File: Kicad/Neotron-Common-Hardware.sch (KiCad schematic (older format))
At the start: 12 parts

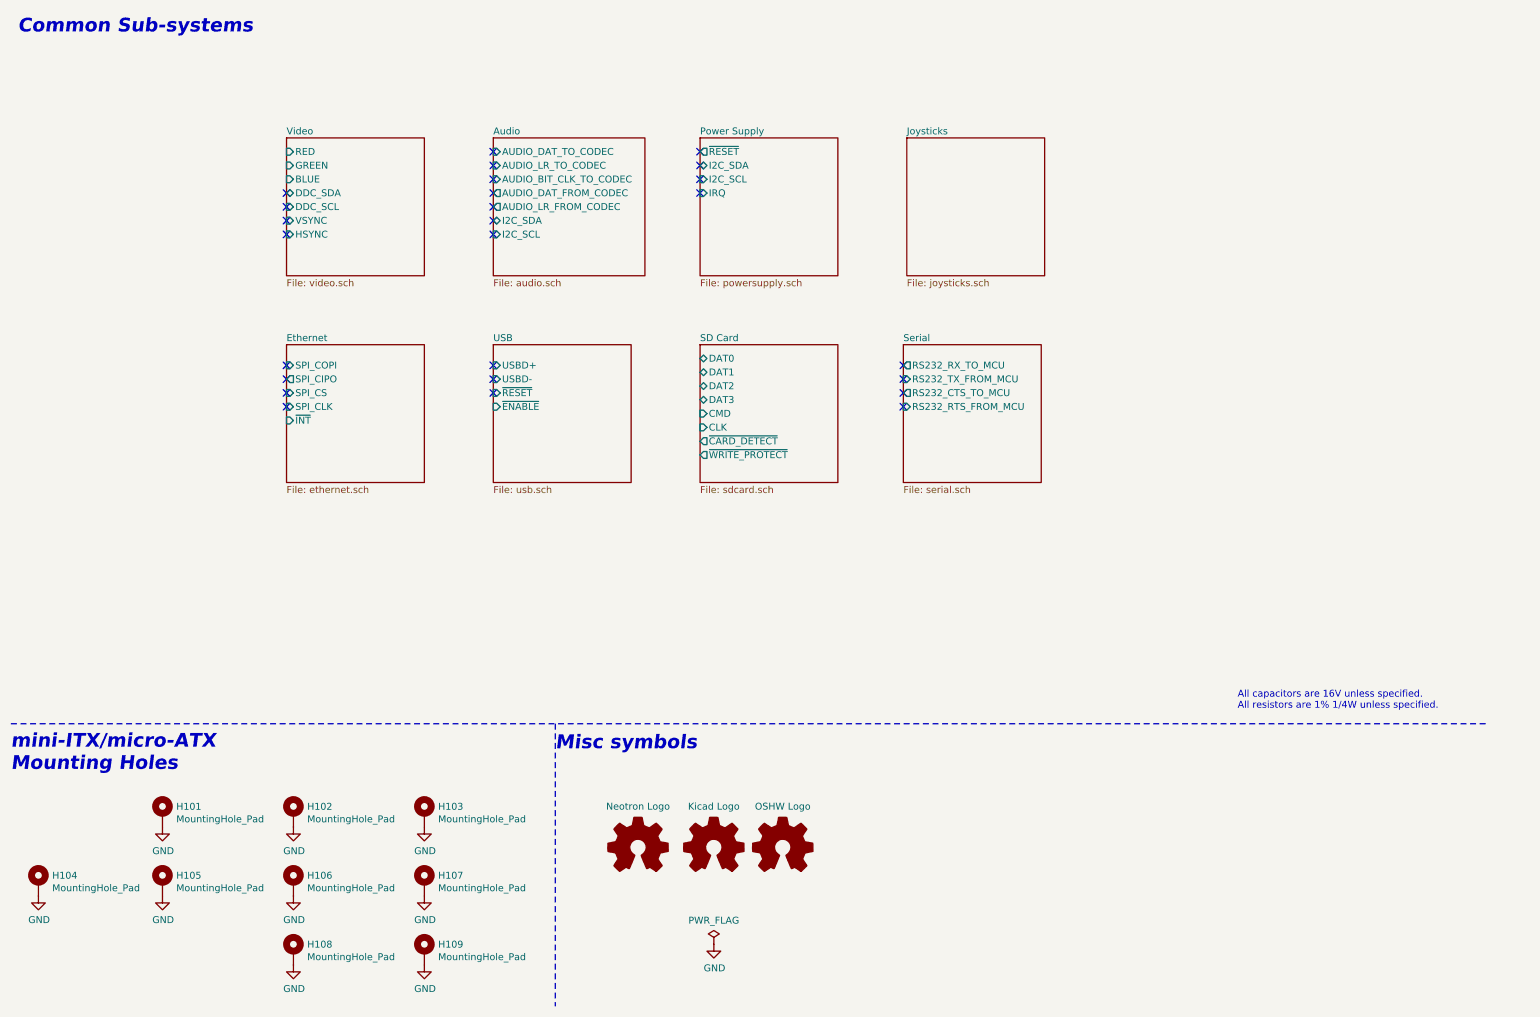
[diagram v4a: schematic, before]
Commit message: Make CPU card bigger.
Just big enough to take a TQFP-176 now.
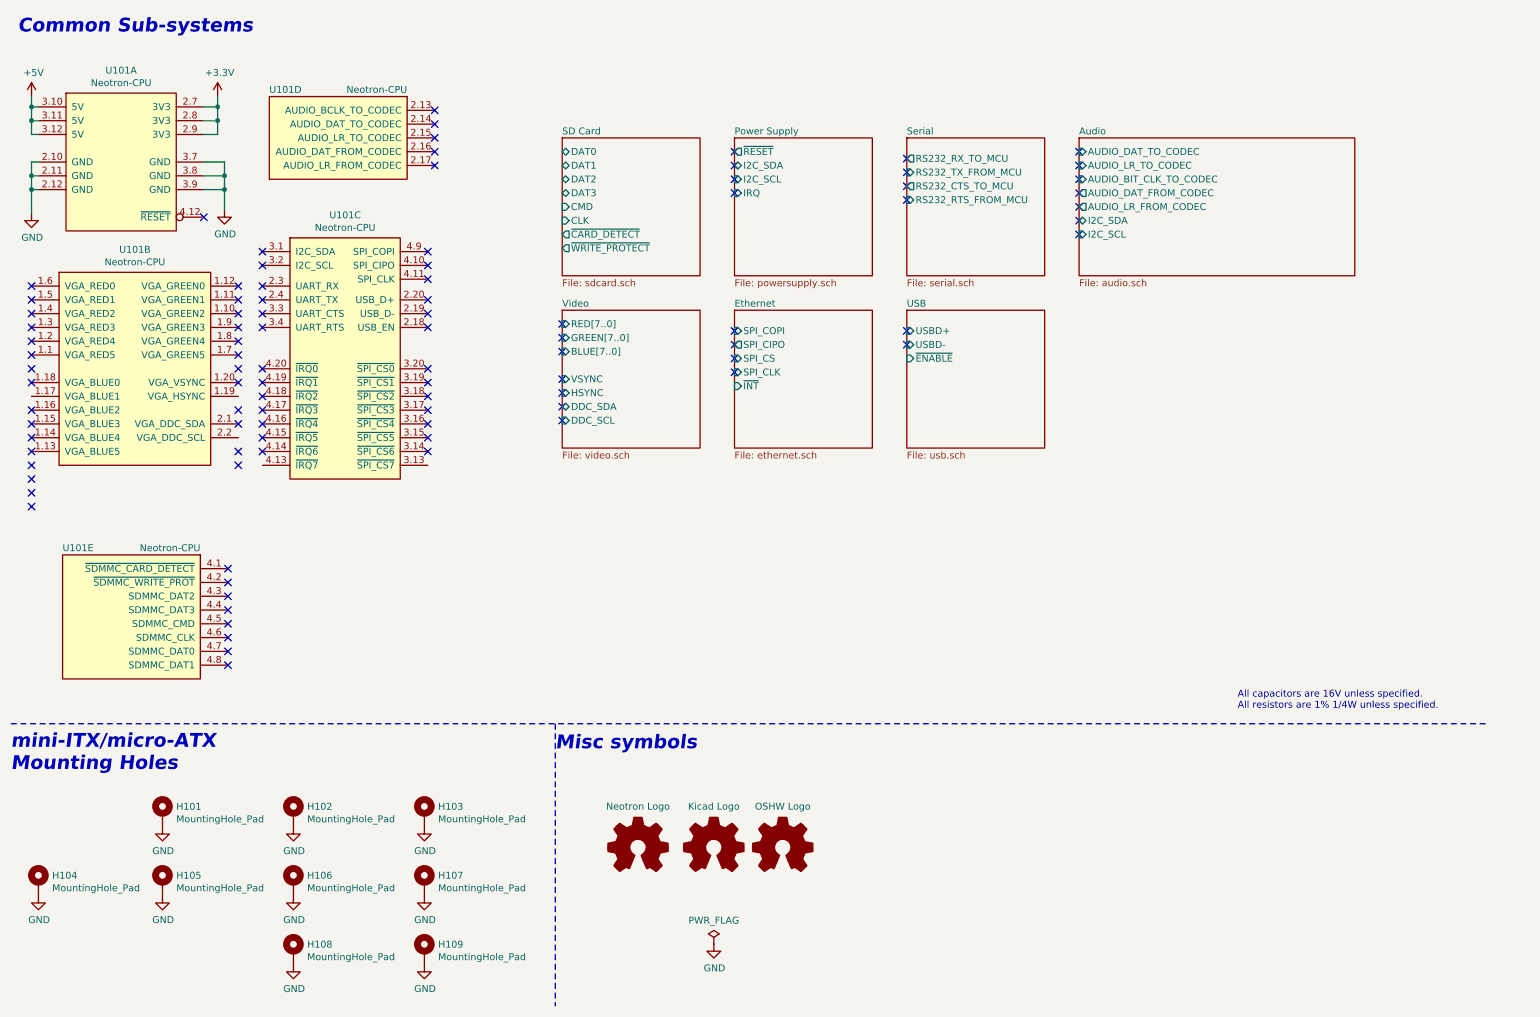
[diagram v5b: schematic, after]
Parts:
- added U101: Neotron-CPU, Neotron-Common-Hardware:Neotron_CPU_Socket, symbol Neotron-Common-Hardware:Neotron-CPU
- LOGO101, LOGO102, LOGO103: DNP 0 -> 1
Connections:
- net GND: now also U101.2.10 (GND), U101.2.11 (GND), U101.2.12 (GND), U101.3.7 (GND), U101.3.8 (GND), U101.3.9 (GND)
- new net +3V3: U101.2.7 (3V3), U101.2.8 (3V3), U101.2.9 (3V3)
- new net +5V: U101.3.10 (5V), U101.3.11 (5V), U101.3.12 (5V)
- no-connect marks 26 -> 96

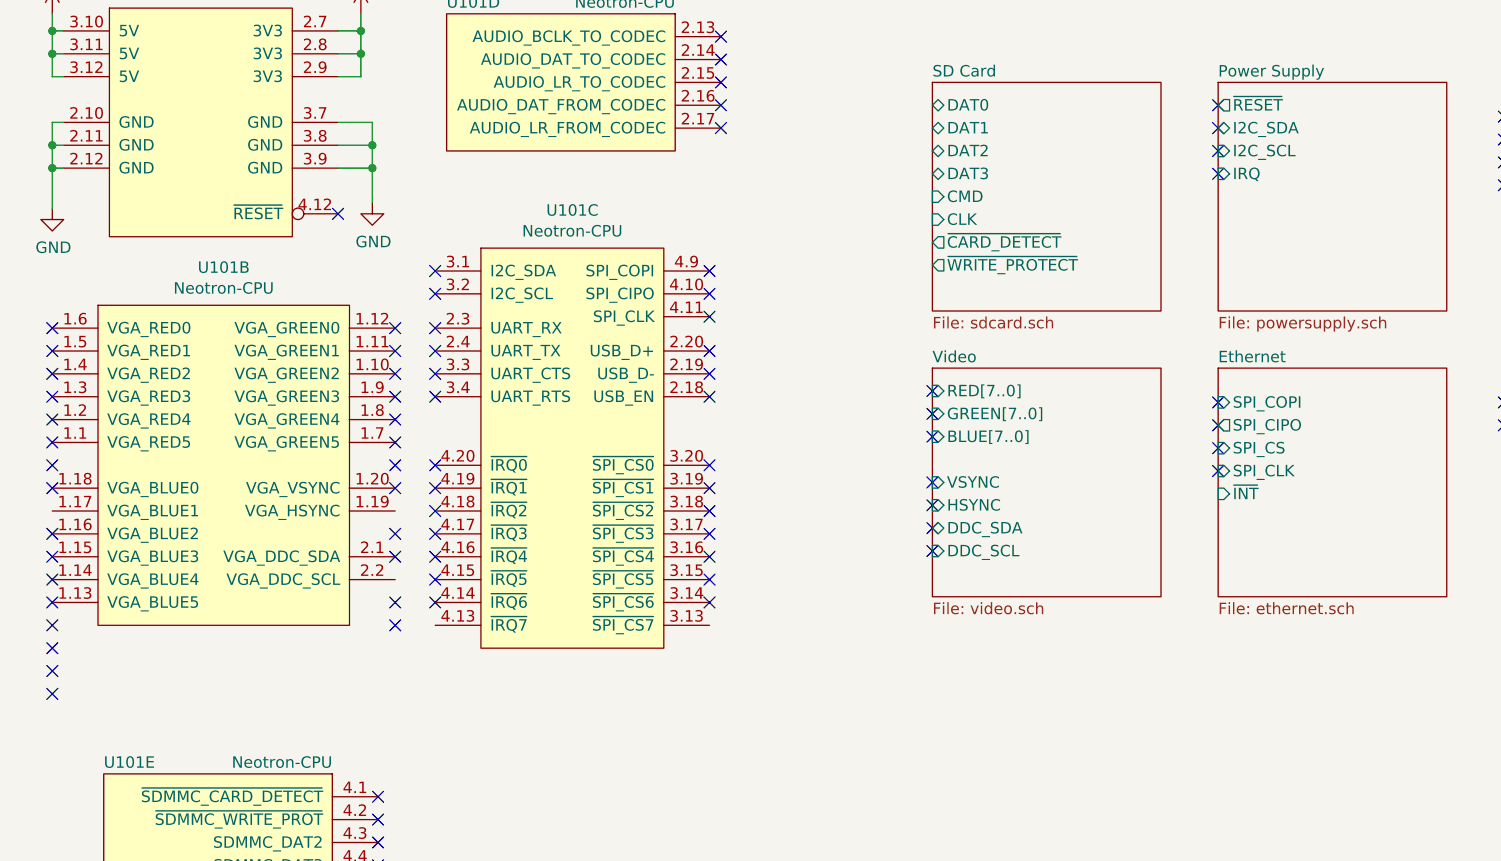
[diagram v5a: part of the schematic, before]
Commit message: Revised CPU connector to be two 2x20.
This gives more room for larger TQFP-176+ CPUs to be fitted that
didn't fit on the PGA-80 design.
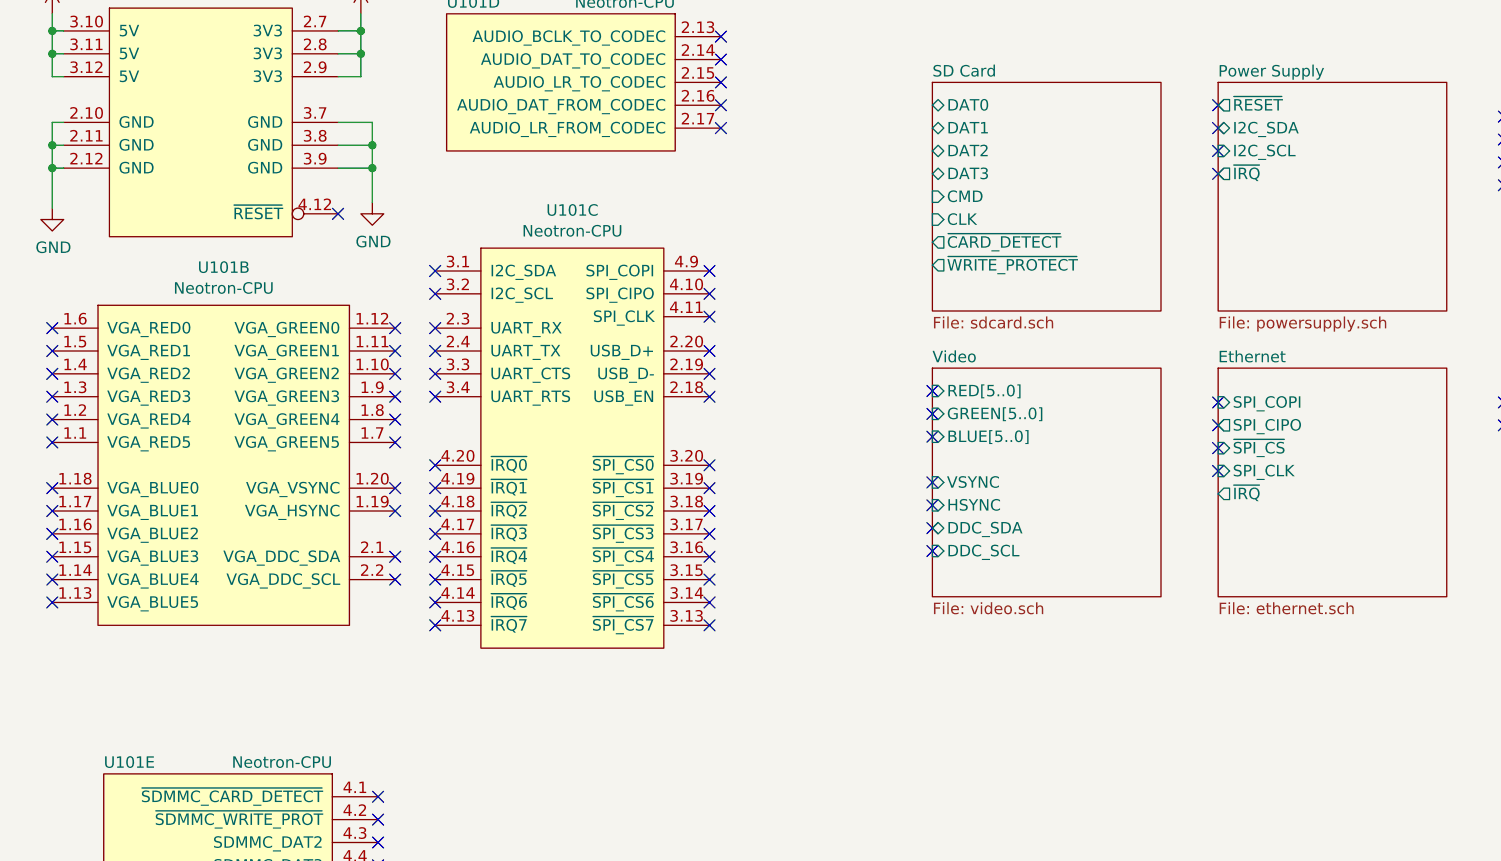
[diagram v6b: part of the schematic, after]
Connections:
- no-connect marks 96 -> 92
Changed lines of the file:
@@
 F4 "VSYNC" I L 4500 3250 50
 F5 "HSYNC" I L 4500 3350 50
-F6 "RED[7..0]" I L 4500 2850 50
-F7 "GREEN[7..0]" I L 4500 2950 50
-F8 "BLUE[7..0]" I L 4500 3050 50
+F6 "RED[5..0]" I L 4500 2850 50
+F7 "GREEN[5..0]" I L 4500 2950 50
+F8 "BLUE[5..0]" I L 4500 3050 50
 $EndSheet
 $Sheet
@@
 F3 "I2C_SDA" B L 5750 1700 50
 F4 "I2C_SCL" I L 5750 1800 50
-F5 "IRQ" I L 5750 1900 50
+F5 "~IRQ" O L 5750 1900 50
 $EndSheet
 $Sheet
@@
 F2 "SPI_COPI" I L 5750 2900 50
 F3 "SPI_CIPO" O L 5750 3000 50
-F4 "SPI_CS" I L 5750 3100 50
+F4 "~SPI_CS" I L 5750 3100 50
 F5 "SPI_CLK" I L 5750 3200 50
-F6 "~INT" I L 5750 3300 50
+F6 "~IRQ" O L 5750 3300 50
 $EndSheet
 $Comp
@@
 NoConn ~ 2150 2975
 NoConn ~ 2150 3075
-NoConn ~ 2150 3175
+NoConn ~ 2150 3375
 NoConn ~ 2150 3275
-NoConn ~ 2150 3475
 NoConn ~ 2150 3575
-NoConn ~ 2150 3775
-NoConn ~ 2150 3875
 NoConn ~ 650  2575
 NoConn ~ 650  2675
@@
 NoConn ~ 650  2975
 NoConn ~ 650  3075
-NoConn ~ 650  3175
 NoConn ~ 650  3275
 NoConn ~ 650  3475
@@
 NoConn ~ 650  3675
 NoConn ~ 650  3775
-NoConn ~ 650  3875
-NoConn ~ 650  3975
-NoConn ~ 650  4075
-NoConn ~ 650  4175
+NoConn ~ 650  3375
 NoConn ~ 2075 4625
 NoConn ~ 2075 4725
@@
 NoConn ~ 4500 3450
 NoConn ~ 4500 3550
+NoConn ~ 2150 3675
+NoConn ~ 2325 3875
+NoConn ~ 3525 3875
 $EndSCHEMATC

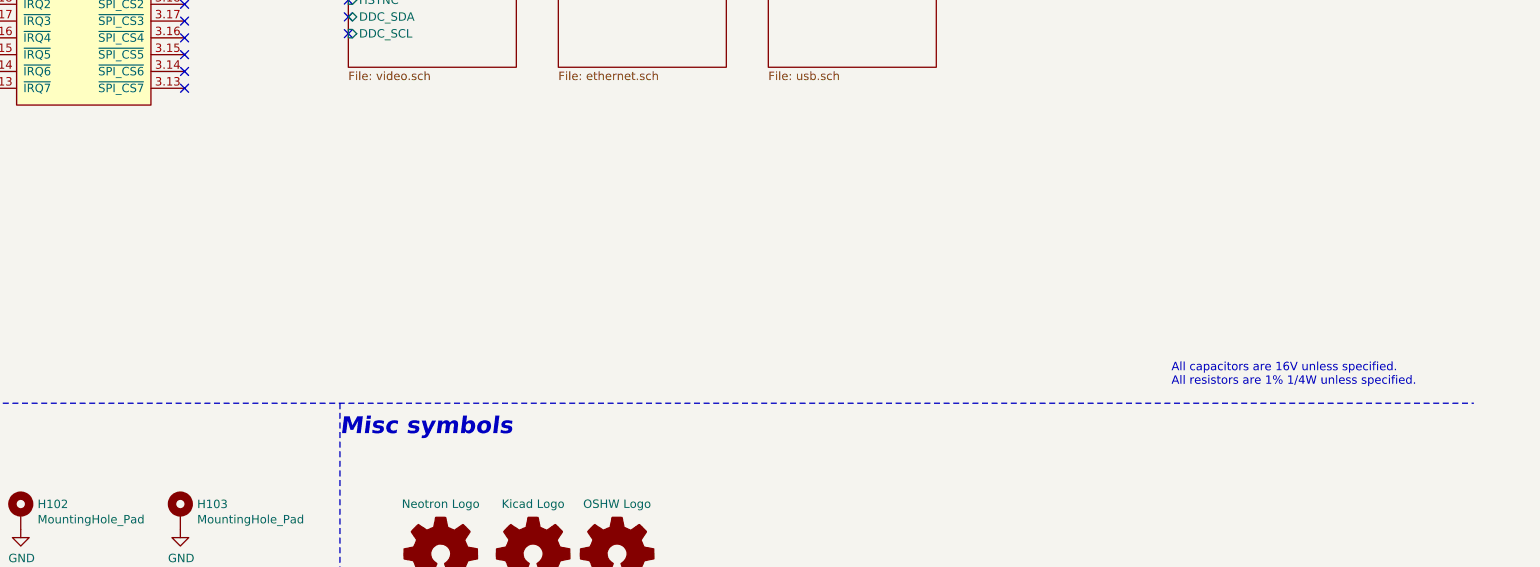
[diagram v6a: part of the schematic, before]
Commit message: Changed CPU socket to be 2x20 x2. Added expansion slots.
Also added 3D model for the SD card.
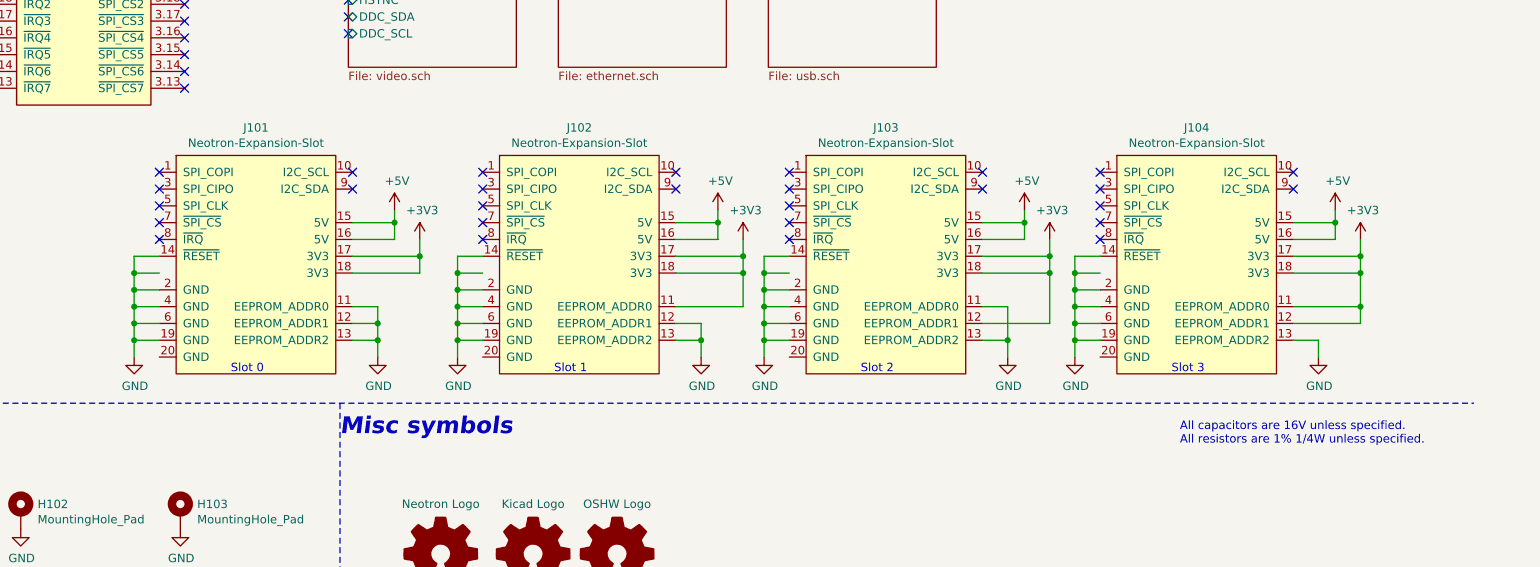
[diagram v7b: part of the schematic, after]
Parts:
- added J101, J102, J103, J104: Neotron-Expansion-Slot, Neotron-Common-Hardware:Neotron-Expansion-Slot, symbol Neotron-Common-Hardware:Neotron-Expansion-Slot
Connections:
- net labels added: +3V3
- wire segments 24 -> 128
- no-connect marks 92 -> 120
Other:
- note added: "Slot 0"
- note added: "Slot 1"
- note added: "Slot 2"
- note added: "Slot 3"
